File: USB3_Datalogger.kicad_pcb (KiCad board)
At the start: 6 copper layers, 68.5 x 53.5 mm, 82 parts, among them J101 Conn_02x20_Odd_Even, J102 Conn_02x07_Odd_Even, J201 USB3-micro, J301 Conn_01x07, SW101 SW_Push, SW102 SW_Push, U101 ASDMB-xxxMHz, U201 FT600, U202 TPD2EUSB30, U203 TPD2EUSB30, U204 USB6B1, U301 ICE40HX1K-4K-TQ144, U302 W25Q32JVZP, U401 tps6240x, U402 TLV73325PDBV, Y201 30MHz

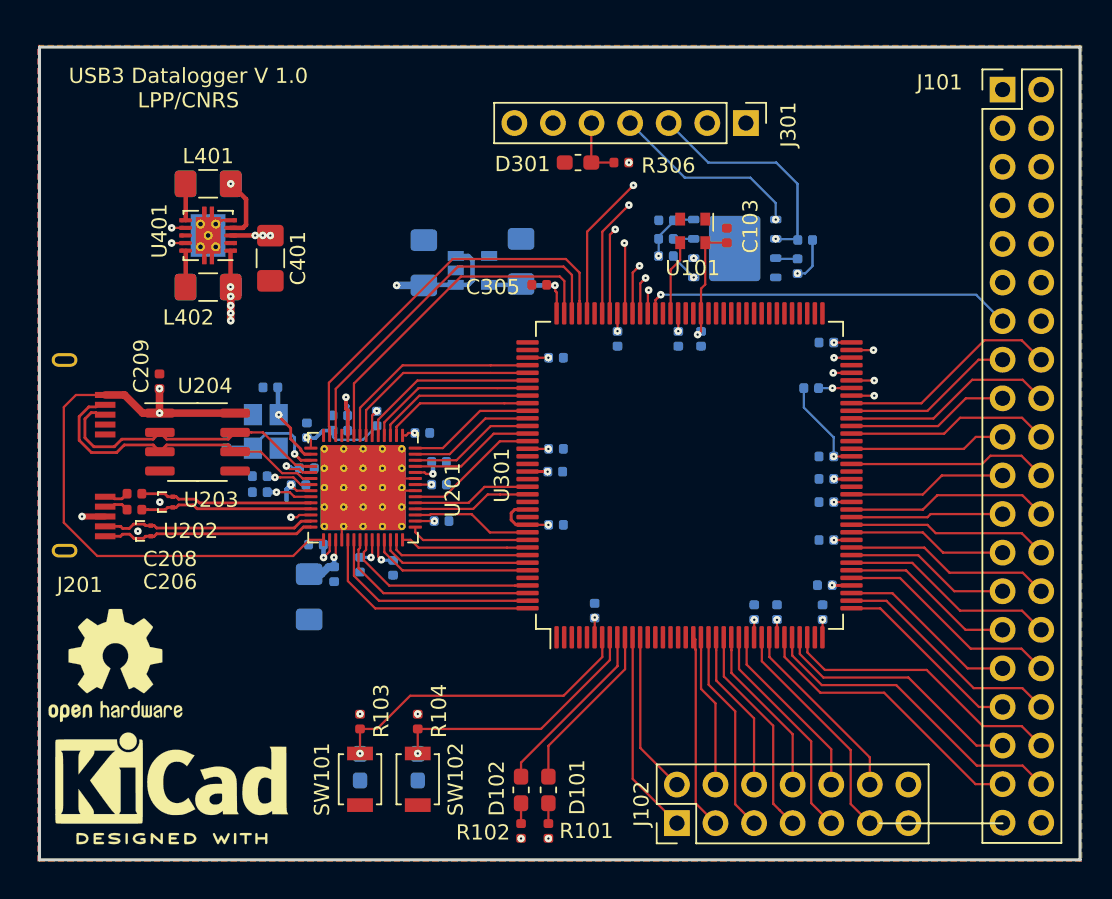
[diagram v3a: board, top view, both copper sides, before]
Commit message: Added STM32F1 as FPGA companion
Signed-off-by: Alexis Jeandet <alexis.jeandet@member.fsf.org>
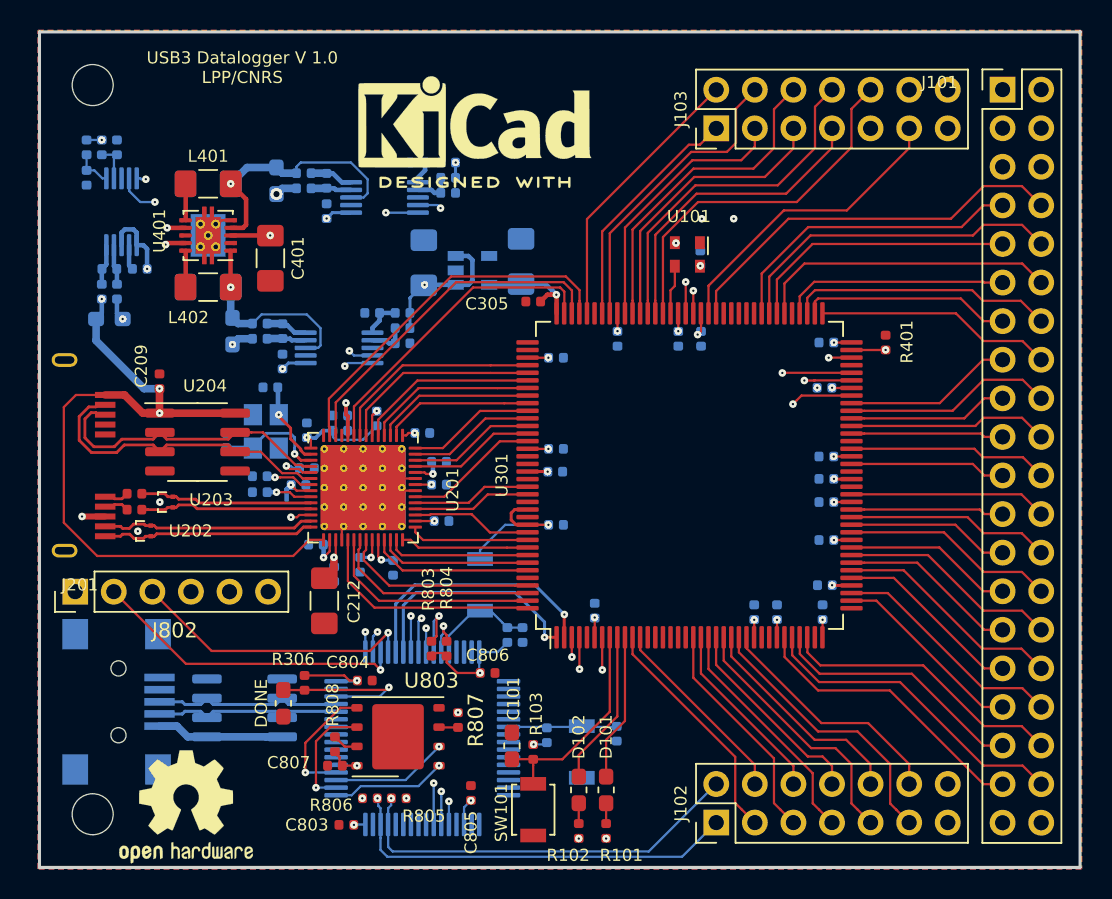
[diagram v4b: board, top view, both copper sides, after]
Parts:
- removed C102: C, Capacitor_SMD:C_0603_1608Metric_Pad1.05x0.95mm_HandSolder
- removed C304: 100nF, Capacitor_SMD:C_0402_1005Metric
- removed D301: LED, Resistor_SMD:R_0603_1608Metric_Pad1.05x0.95mm_HandSolder
- removed J301: Conn_01x07, Connector_PinHeader_2.54mm:PinHeader_1x07_P2.54mm_Vertical
- removed R104: 2K2, Resistor_SMD:R_0402_1005Metric
- removed R301, R302, R303, R304: 10k, Resistor_SMD:R_0402_1005Metric
- removed REF**: KiCad-Logo2_6mm_SilkScreen, Symbol:KiCad-Logo2_6mm_SilkScreen
- removed REF**: OSHW-Logo2_9.8x8mm_SilkScreen, Symbol:OSHW-Logo2_9.8x8mm_SilkScreen
- removed SW102: SW_Push, Button_Switch_SMD:SW_SPST_B3U-1000P
- removed U302: W25Q32JVZP, Package_SON:WSON-8-1EP_6x5mm_P1.27mm_EP3.4x4.3mm
- added BOOT0: SW_Push, Button_Switch_SMD:SW_SPST_B3U-1000P, B.Cu at (111.5, 176.4)
- added C320: 100nF, Capacitor_SMD:C_0402_1005Metric, B.Cu at (89.1, 155.6)
- added C321: 10pF, Capacitor_SMD:C_0402_1005Metric, B.Cu at (87.1, 155.6)
- added C601: 100nF, Capacitor_SMD:C_0402_1005Metric, B.Cu at (101.4, 151.8)
- added C602: 10pF, Capacitor_SMD:C_0402_1005Metric, B.Cu at (101.4, 149.8)
- added C701: 100nF, Capacitor_SMD:C_0402_1005Metric, B.Cu at (98.5, 161.7)
- added C702: 10pF, Capacitor_SMD:C_0402_1005Metric, B.Cu at (98.5, 159.7)
- added C801: C, Capacitor_SMD:C_0402_1005Metric, B.Cu at (113.3, 179.7)
- added C802: C, Capacitor_SMD:C_0402_1005Metric, B.Cu at (120.5, 186.2)
- added C803: 100nF, Capacitor_SMD:C_0402_1005Metric, F.Cu at (102.7, 192.2)
- added C804: 100nF, Capacitor_SMD:C_0402_1005Metric, F.Cu at (103.9, 182.7)
- added C805: 100nF, Capacitor_SMD:C_0402_1005Metric, F.Cu at (110.9, 190.1)
- added C806: 100nF, Capacitor_SMD:C_0402_1005Metric, F.Cu at (112.0, 182.2)
- added C807: 100nF, Capacitor_SMD:C_0402_1005Metric, F.Cu at (102.0, 188.3)
- added DONE401: LED, Resistor_SMD:R_0603_1608Metric_Pad1.05x0.95mm_HandSolder, F.Cu at (98.5, 184.2)
- added H101: MountingHole, MountingHole:MountingHole_2.7mm_M2.5, F.Cu at (86.0, 191.5)
- added H102: MountingHole, MountingHole:MountingHole_2.7mm_M2.5, F.Cu at (86.0, 143.5)
- added J103: Conn_02x07_Odd_Even, Connector_PinHeader_2.54mm:PinHeader_2x07_P2.54mm_Vertical, F.Cu at (127.0, 146.3)
- added J801: USB_B_Mini, Connector_USB:USB_Mini-B_Lumberg_2486_01_Horizontal, B.Cu at (87.7, 184.1)
- added J802: Conn_01x06, Connector_PinHeader_2.54mm:PinHeader_1x06_P2.54mm_Vertical, F.Cu at (84.8, 176.8)
- added LOGO101: Logo_Open_Hardware_Small, Symbol:OSHW-Logo2_9.8x8mm_SilkScreen, F.Cu at (92.2, 191.0)
- added LOGO102: Logo_Open_Hardware_Small, Symbol:KiCad-Logo2_6mm_SilkScreen, F.Cu at (111.2, 145.9)
- added R307: 100m, Capacitor_SMD:C_0603_1608Metric_Pad1.05x0.95mm_HandSolder, B.Cu at (87.1, 158.9)
- added R308: 10, Resistor_SMD:R_0402_1005Metric, B.Cu at (86.6, 157.1)
- added R309: 10, Resistor_SMD:R_0402_1005Metric, B.Cu at (87.6, 157.1)
- added R310: 10k, Capacitor_SMD:C_0402_1005Metric, B.Cu at (85.6, 147.6)
- added R311: 10k, Capacitor_SMD:C_0402_1005Metric, B.Cu at (85.6, 149.6)
- added R312: 10k, Capacitor_SMD:C_0402_1005Metric, B.Cu at (86.6, 147.6)
- added R313: 10k, Capacitor_SMD:C_0402_1005Metric, B.Cu at (87.6, 147.6)
- added R401: 10k, Resistor_SMD:R_0402_1005Metric, F.Cu at (138.2, 160.4)
- added R601: 100m, Capacitor_SMD:C_0603_1608Metric_Pad1.05x0.95mm_HandSolder, B.Cu at (98.1, 149.8)
- added R602: 10, Resistor_SMD:R_0402_1005Metric, B.Cu at (99.9, 149.3)
- added R603: 10, Resistor_SMD:R_0402_1005Metric, B.Cu at (99.9, 150.3)
- added R604: 10k, Capacitor_SMD:C_0402_1005Metric, B.Cu at (109.4, 148.6)
- added R605: 10k, Capacitor_SMD:C_0402_1005Metric, B.Cu at (107.4, 148.6)
- added R606: 10k, Capacitor_SMD:C_0402_1005Metric, B.Cu at (109.4, 149.6)
- added R607: 10k, Capacitor_SMD:C_0402_1005Metric, B.Cu at (109.4, 150.6)
- added R701: 100m, Capacitor_SMD:C_0603_1608Metric_Pad1.05x0.95mm_HandSolder, B.Cu at (95.2, 159.7)
- added R702: 10, Resistor_SMD:R_0402_1005Metric, B.Cu at (97.0, 159.2)
- added R703: 10, Resistor_SMD:R_0402_1005Metric, B.Cu at (97.0, 160.2)
- added R704: 10k, Capacitor_SMD:C_0402_1005Metric, B.Cu at (106.4, 158.5)
- added R705: 10k, Capacitor_SMD:C_0402_1005Metric, B.Cu at (104.4, 158.5)
- added R706: 10k, Capacitor_SMD:C_0402_1005Metric, B.Cu at (106.4, 159.5)
- added R707: 10k, Capacitor_SMD:C_0402_1005Metric, B.Cu at (106.4, 160.5)
- added R801: 2K2, Resistor_SMD:R_0402_1005Metric, B.Cu at (114.3, 179.7)
- added R802: 2K2, Resistor_SMD:R_0402_1005Metric, B.Cu at (115.9, 186.3)
- added R803: 2K2, Resistor_SMD:R_0402_1005Metric, F.Cu at (108.3, 180.6)
- added R804: 2K2, Resistor_SMD:R_0402_1005Metric, F.Cu at (109.3, 180.6)
- added R805: 2K2, Resistor_SMD:R_0402_1005Metric, F.Cu at (106.2, 190.4)
- added R806: 2K2, Resistor_SMD:R_0402_1005Metric, F.Cu at (104.2, 190.4)
- added R807: 10k, Resistor_SMD:R_0402_1005Metric, F.Cu at (110.0, 185.3)
- added R808: 10k, Resistor_SMD:R_0402_1005Metric, F.Cu at (102.0, 186.9)
- added RST0: SW_Push, Button_Switch_SMD:SW_SPST_B3U-1000P, B.Cu at (118.2, 187.4)
- added U303: INA226, Package_SO:VSSOP-10_3x3mm_P0.5mm, B.Cu at (87.9, 151.8)
- added U601: INA226, Package_SO:VSSOP-10_3x3mm_P0.5mm, B.Cu at (105.2, 150.9)
- added U701: INA226, Package_SO:VSSOP-10_3x3mm_P0.5mm, B.Cu at (102.2, 160.8)
- added U801: STM32F103RCTx, Package_QFP:LQFP-64_10x10mm_P0.5mm, B.Cu at (107.7, 186.5)
- added U802: USB6B1, Package_SO:SOIC-8_3.9x4.9mm_P1.27mm, B.Cu at (96.0, 184.5)
- added U803: W25Q32JVZP, Package_SON:WSON-8-1EP_6x5mm_P1.27mm_EP3.4x4.3mm, F.Cu at (106.1, 186.4)
- C101, C212: moved to F.Cu
- C103: moved to B.Cu
- moved R306 40.1 mm to (100.0, 182.8), turned to 270 degrees
- moved R103 11.6 mm to (115.0, 187.4)
- moved SW101 11.6 mm to (115.0, 191.2)
- moved C101 10.1 mm to (113.6, 187.0), turned to 90 degrees
- moved D101 3.80 mm to (119.8, 189.9)
- moved D102 3.80 mm to (118.0, 189.9)
- moved R101 3.80 mm to (119.8, 192.6)
- moved R102 3.80 mm to (118.0, 192.6)
- moved J102 2.59 mm to (127.0, 192.1)
- moved C103 2.30 mm to (126.0, 154.9)
- moved U101 1.59 mm to (125.2, 154.7)
- moved C305 1.17 mm to (115.0, 157.8)
- moved C212 1.03 mm to (101.2, 177.4)
- moved R305 0.88 mm to (134.2, 163.4)
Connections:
- net /Sheet5E4285EB/2.5V renamed /2.5V
- net /Sheet5E4285EB/FLASH_CDONE renamed /STM32/FLASH_CDONE
- net /Sheet5E4285EB/FLASH_~CRESET renamed /STM32/FLASH_~CRESET
- C101 pad 1: /IOL_4 -> /IOL_5
- C209 pad 1: /VBUS -> /Sheet5E41F9C9/VBUS
- C401 pad 1: /VBUS -> /USB_5V
- C402 pad 1: VCCIO_0 -> /Sheet5F0E3366/#3.3V
- C403 pad 1: VCC -> /Sheet5F0E3366/#1.2V
- C404 pad 1: /VBUS -> /USB_5V
- J101 pad 10: /IOR_19 -> /IOR_6
- J101 pad 11: /IOR_16 -> /IOR_3
- J101 pad 12: /IOR_17 -> /IOR_4
- J101 pad 13: /IOR_14 -> /IOR_1
- J101 pad 14: /IOR_15 -> /IOR_2
- J101 pad 15: /IOB_18 -> /IOB_19
- J101 pad 16: /IOB_19 -> /IOR_0
- J101 pad 17: /IOB_16 -> /IOB_17
- J101 pad 18: /IOB_17 -> /IOB_18
- J101 pad 19: /IOB_14 -> /IOB_15
- J101 pad 20: /IOB_15 -> /IOB_16
- J101 pad 21: /IOB_12 -> /IOB_13
- J101 pad 22: /IOB_13 -> /IOB_14
- J101 pad 23: /IOB_10 -> /IOB_11
- J101 pad 24: /IOB_11 -> /IOB_12
- J101 pad 25: /IOB_8 -> /IOB_9
- J101 pad 26: /IOB_9 -> /IOB_10
- J101 pad 27: /IOB_6 -> /IOB_7
- J101 pad 28: /IOB_7 -> /IOB_8
- J101 pad 29: /IOB_4 -> /IOB_5
- J101 pad 3: /VBUS -> /USB_5V
- J101 pad 30: /IOB_5 -> /IOB_6
- J101 pad 31: /IOB_2 -> /IOB_3
- J101 pad 32: /IOB_3 -> /IOB_4
- J101 pad 33: /IOB_0 -> /IOB_1
- J101 pad 34: /IOB_1 -> /IOB_2
- J101 pad 4: /VBUS -> /USB_5V
- J101 pad 7: /IOR_20 -> /IOR_7
- J101 pad 8: /IOR_21 -> /IOR_8
- J101 pad 9: /IOR_18 -> /IOR_5
- J102 pad 1: /IOL_8 -> /Ext_I2C_SDA
- J102 pad 10: /IOL_17 -> /IOL_15
- J102 pad 11: /IOL_18 -> /IOL_16
- J102 pad 12: /IOL_19 -> /IOL_17
- J102 pad 2: /IOL_9 -> /Ext_I2C_SCL
- J102 pad 3: /IOL_10 -> /IOL_8
- J102 pad 4: /IOL_11 -> /IOL_9
- J102 pad 5: /IOL_12 -> /IOL_10
- J102 pad 6: /IOL_13 -> /IOL_11
- J102 pad 7: /IOL_14 -> /IOL_12
- J102 pad 8: /IOL_15 -> /IOL_13
- J102 pad 9: /IOL_16 -> /IOL_14
- J201 pad 1: /VBUS -> /Sheet5E41F9C9/VBUS
- L401 pad 2: VCC -> /Sheet5F0E3366/#1.2V
- L402 pad 2: VCCIO_0 -> /Sheet5F0E3366/#3.3V
- R103 pad 2: /IOL_4 -> /IOL_5
- SW101 pad 2: /IOL_4 -> /IOL_5
- U201 pad 29: /VBUS -> /Sheet5E41F9C9/VBUS
- U204 pad 1: /VBUS -> /Sheet5E41F9C9/VBUS
- U204 pad 8: /VBUS -> /Sheet5E41F9C9/VBUS
- U301 pad 67: /Sheet5E4285EB/FLASH_MOSI -> /Sheet5E4285EB/FLASH_MISO
- U301 pad 68: /Sheet5E4285EB/FLASH_MISO -> /Sheet5E4285EB/FLASH_MOSI
- U301 pad 71: /Sheet5E4285EB/FLASH_~CS -> /Sheet5E4285EB/FLASH_SS
- U401 pad 1: VCCIO_0 -> /Sheet5F0E3366/#3.3V
- U401 pad 3: /VBUS -> /USB_5V
- U401 pad 4: VCC -> /Sheet5F0E3366/#1.2V
- U401 pad 7: /VBUS -> /USB_5V
- U401 pad 9: /VBUS -> /USB_5V
- U402 pad 1: /VBUS -> /USB_5V
- U402 pad 3: /VBUS -> /USB_5V
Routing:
- net /VBUS: track 135.2 -> 0.00 mm, vias 8 -> 0
- net /USB_5V: track 0.00 -> 133.4 mm, vias 0 -> 8
- net /Sheet5E41F9C9/VBUS: track 0.00 -> 69.2 mm, vias 0 -> 5
- net /STM32/Int_SDA: track 0.00 -> 62.5 mm, vias 0 -> 4
- net /STM32/Int_SCL: track 0.00 -> 62.4 mm, vias 0 -> 4
- net /Sheet5E4285EB/FLASH_SS: track 0.00 -> 44.8 mm, vias 0 -> 2
- net VCCIO_0: track 37.3 -> 70.2 mm, vias 21 -> 23
- net /Ext_I2C_SCL: track 0.00 -> 26.8 mm, vias 0 -> 1
- net /Ext_I2C_SDA: track 0.00 -> 26.7 mm, vias 0 -> 1
- net /IOR_8: track 0.00 -> 26.3 mm
- net /Sheet5E4285EB/FLASH_~CS: track 25.6 -> 0.00 mm, vias 2 -> 0
- net /IOR_13: track 0.00 -> 24.2 mm
- net /IOR_10: track 0.00 -> 22.4 mm, vias 0 -> 1
- net /IOR_6: track 0.00 -> 22.3 mm
- net /STM32/UART4_TX: track 0.00 -> 20.9 mm, vias 0 -> 1
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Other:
- board size 68.5 x 53.5 mm -> 68.5 x 55 mm

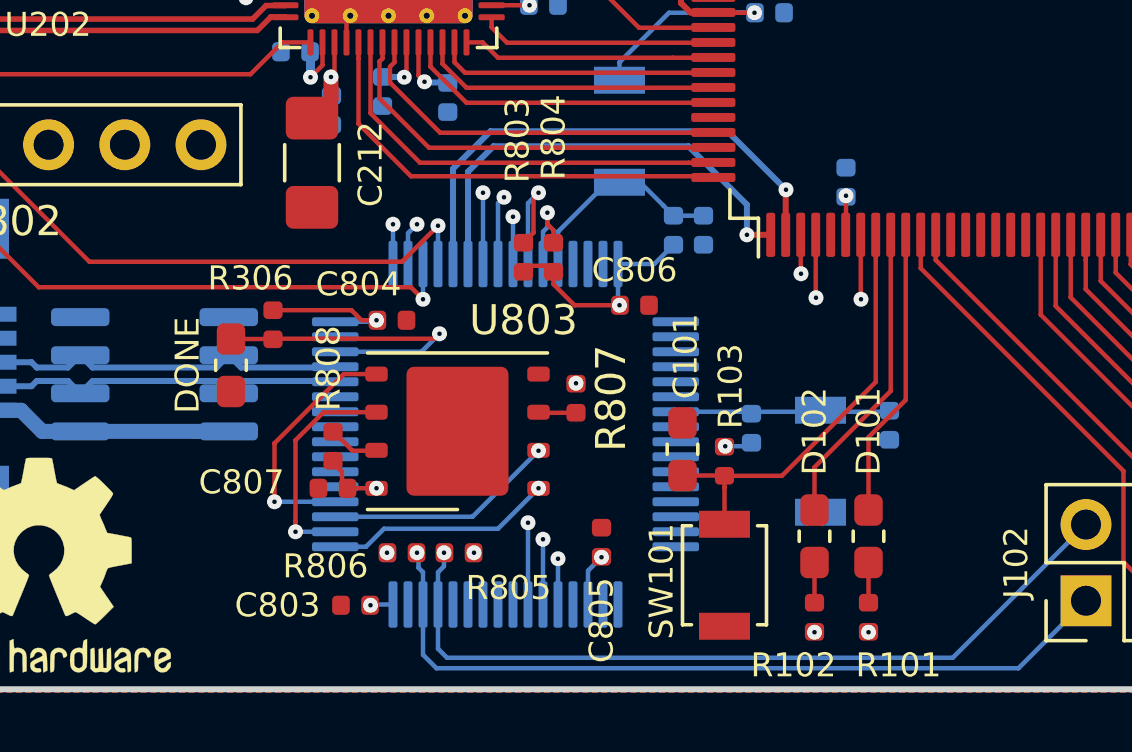
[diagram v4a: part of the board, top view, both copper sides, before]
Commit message: STM32 connected VDDA to 3.3V
Signed-off-by: Alexis Jeandet <alexis.jeandet@member.fsf.org>
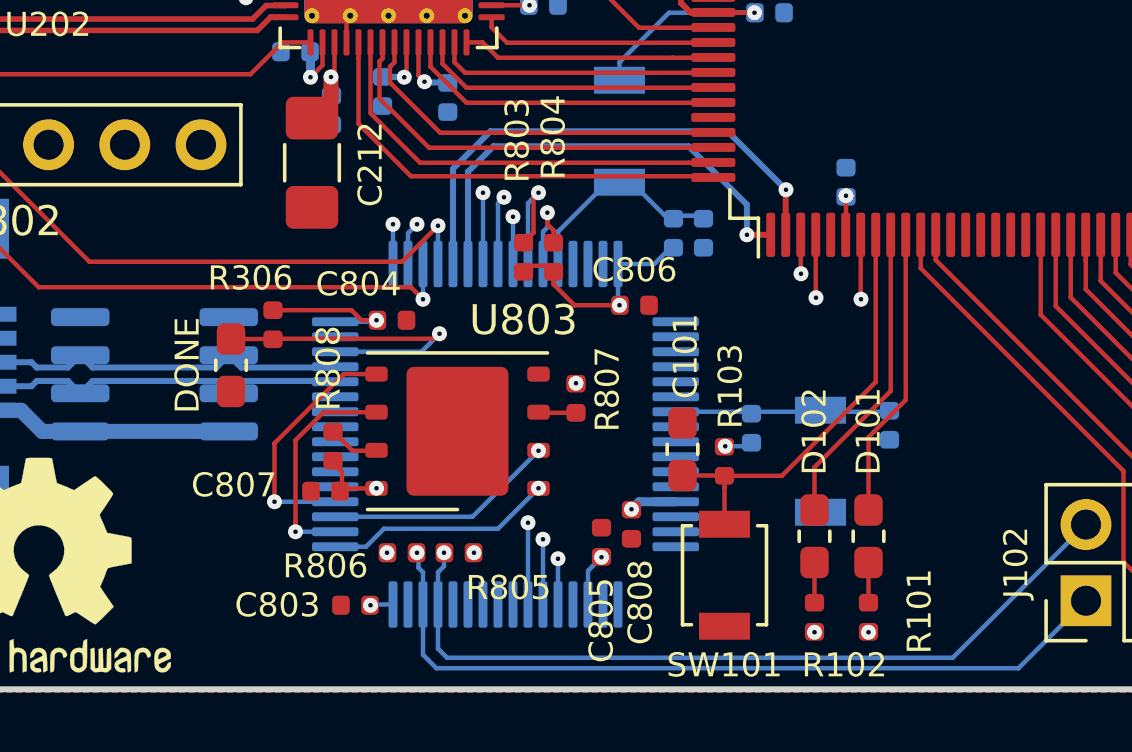
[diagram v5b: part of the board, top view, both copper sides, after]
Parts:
- added C808: 100nF, Capacitor_SMD:C_0402_1005Metric, F.Cu at (111.9, 189.5)
- moved C807 0.27 mm to (101.7, 188.4)
- moved C801 0.10 mm to (113.3, 179.8)
- moved R801 0.10 mm to (114.3, 179.8)
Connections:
- U801 pad 13: Net-(U801-Pad13) -> VCCIO_0
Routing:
- net VCCIO_0: track 70.2 -> 72.0 mm, vias 23 -> 24
- net VCC: track 33.6 -> 34.5 mm

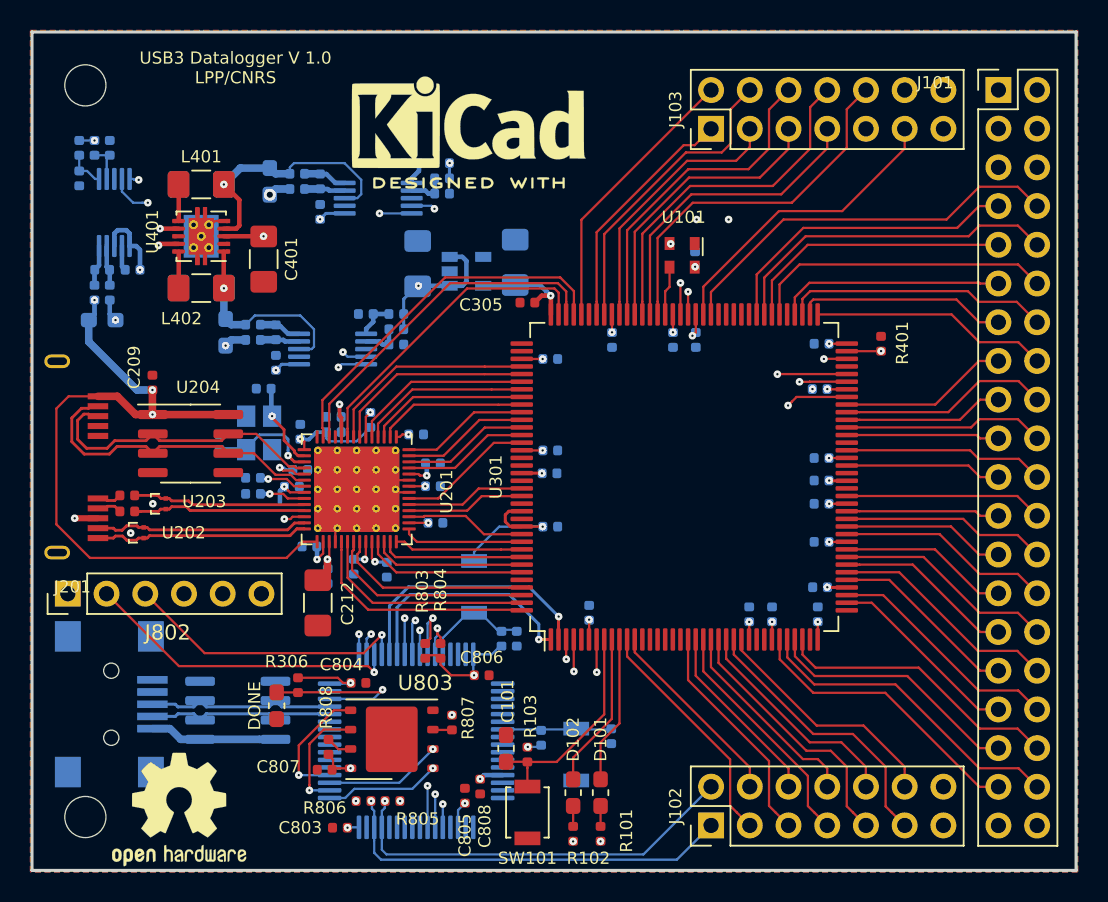
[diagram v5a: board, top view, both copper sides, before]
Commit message: Added many GND vias
Signed-off-by: Alexis Jeandet <alexis.jeandet@member.fsf.org>
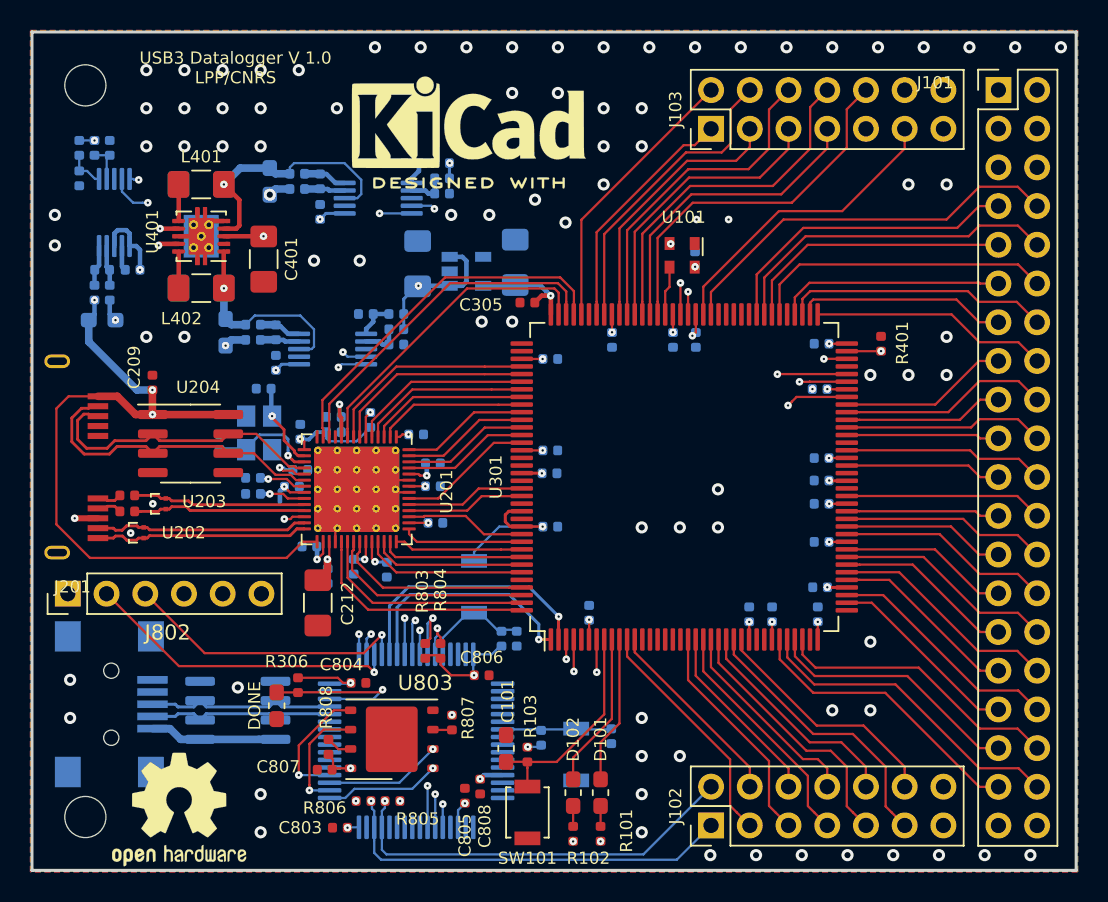
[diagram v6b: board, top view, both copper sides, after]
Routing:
- net GND: track 16.3 -> 18.8 mm, vias 6 -> 86
